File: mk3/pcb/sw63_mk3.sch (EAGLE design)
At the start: 62 parts, among them J1 USB-C_2.0_SMT, Q1 LGE2305, Q2 BC817S, Q3 BC817S, SW1 KSC321JLFS, SW2 EVQ-P7J01P, U1 ATSAMD21E18A-MU, U2 DS3231MZ+, U3 TLC5916IPW, U4 TLC5916IPW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

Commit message: finishing schematics
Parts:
- removed LD13, LD14, LD15, LD16: (no value), BASTL_LEDS:LED_THT-5MM_ALT
- removed LD17, LD18, LD19, LD20: LED_RECT-3.2X2, BASTL_LEDS:LED_RECT-3.2X2
- removed LD21: (no value), BASTL_LEDS:LED_THT-3MM_ALT
- removed LD22: LED_SMT_0805, BASTL_LEDS:LED_SMT_0805
- added B+, B-: TEST_PIN_LARGE, BASTL_PINHEADERS:TEST_PIN_LARGE
- added DOWN, LEFT, RIGHT, UP: LED_RECT-3.2X2, BASTL_LEDS:LED_RECT-3.2X2
- added HOURS, MINUS, MINUTES, PLUS: (no value), BASTL_LEDS:LED_THT-5MM_ALT
- added PM: (no value), BASTL_LEDS:LED_THT-3MM_ALT
- added Q4: TEMT6200FX01, BASTL_TRANZISTORS:TEMT6200FX01
- added R14: 10k, BASTL_RESISTORS:RESISTOR0603
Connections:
- new net LIGHT_SENS: Q4.E, R14.2, U1.PA02
- new net N$20: LD10.C, U3.OUT1
- new net N$25: LD5.C, U3.OUT7
- new net N$26: C9.2, U1.VDDCORE
- new net N$27: LD4.C, U4.OUT4
- new net N$28: LD3.C, U4.OUT5
- new net N$29: LD2.C, U4.OUT6
- new net N$31: MINUTES.C, U4.OUT3
- new net N$32: HOURS.C, U4.OUT2
- new net N$33: MINUS.C, U4.OUT1
- new net N$34: PLUS.C, U4.OUT0
- new net SCL: R5.2, U1.PA09, U2.SCL
- new net SDA: R6.2, U1.PA08, U2.SDA
- new net SWCLK: SWD.4, U1.PA30
- new net SWDIO: SWD.2, U1.PA31
- net !CHARGING: now also U1.PA10
- net !RESET: now also SWD.3
- net ACTIVE: now also Q4.C, U1.PA03
- net BAT: now also B+.P$1
- net BRIGHT: now also U1.PA18
- net BTN: now also U1.PA00
- net CLK: now also U1.PA07
- net D+: now also U1.PA27
- net D-: now also U1.PA25
- net DAT: now also U1.PA06
- net GND: now also B-.P$1, C10.1, C11.1, C9.1, R14.1, SWD.5, U1.EP, U1.GND
- net LAT: now also U1.PA05
- net N$15: now also PM.C; no longer LD21.C
- net N$16: now also DOWN.C; no longer LD19.C
- net N$17: now also LEFT.C; no longer LD20.C
- net N$18: now also RIGHT.C; no longer LD18.C
- net N$19: now also UP.C; no longer LD17.C
- net N$21: now also LD9.C, U3.OUT0; no longer LD13.C, U3.OUT2
- net N$22: now also LD8.C, U3.OUT4; no longer LD14.C, U3.OUT1
- net N$23: now also LD7.C, U3.OUT5; no longer LD15.C, U3.OUT0
- net N$24: now also LD6.C, U3.OUT6; no longer LD16.C, U3.OUT3
- net N$5: now also LD12.C, U3.OUT3; no longer R6.2, U2.SDA
- net N$7: now also LD11.C, U3.OUT2; no longer R5.2, U2.SCL
- net VBUS_DTCT: now also U1.PA04
- net VDD: now also C10.2, C11.2, SWD.1, U1.VDDANA, U1.VDDIN
- net VDDLEDS: now also DOWN.A, HOURS.A, LEFT.A, MINUS.A, MINUTES.A, PLUS.A, PM.A, RIGHT.A, UP.A; no longer LD13.A, LD14.A, LD15.A, LD16.A, LD17.A, LD18.A, LD19.A, LD20.A, LD21.A
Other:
- moved on the sheet: C10, C11, C9, LD1, LD10, LD11, LD12, LD2, LD3, LD4, LD5, LD6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

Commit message: routing done
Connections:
- net GND: now also U1.PA22
- net N$31: now also HOURS.C; no longer MINUTES.C
- net N$32: now also MINUTES.C; no longer HOURS.C
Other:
- note added: "Just for layout."
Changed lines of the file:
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@@
 <part name="B-" library="BASTL_PINHEADERS" library_urn="urn:adsk.eagle:library:32976504" deviceset="TEST_PIN" device="_LARGE" package3d_urn="urn:adsk.eagle:package:43479613/3" value="TEST_PIN_LARGE"/>
 <part name="GND21" library="BASTL_SYMBOLS" library_urn="urn:adsk.eagle:library:32975873" deviceset="GND" device=""/>
+<part name="GND22" library="BASTL_SYMBOLS" library_urn="urn:adsk.eagle:library:32975873" deviceset="GND" device=""/>
 </parts>
 <sheets>
@@
 <plain>
 <text x="238.76" y="76.2" size="1.27" layer="94" ratio="12">Kinda weird but works.</text>
+<text x="24.384" y="-19.05" size="1.27" layer="94" ratio="12">Just for layout.</text>
 </plain>
 <instances>
@@
 <instance part="GND21" gate="1" x="-99.06" y="2.54" smashed="yes">
 <attribute name="VALUE" x="-101.6" y="0" size="1.778" layer="96"/>
+</instance>
+<instance part="GND22" gate="1" x="35.56" y="-22.86" smashed="yes">
+<attribute name="VALUE" x="33.02" y="-25.4" size="1.778" layer="96"/>
 </instance>
 </instances>
@@
 <pinref part="B-" gate="G$1" pin="P$1"/>
 <pinref part="GND21" gate="1" pin="GND"/>
+</segment>
+<segment>
+<pinref part="U1" gate="G$1" pin="PA22"/>
+<pinref part="GND22" gate="1" pin="GND"/>
+<wire x1="15.24" y1="-20.32" x2="35.56" y2="-20.32" width="0.1524" layer="91"/>
 </segment>
 </net>
@@
 <wire x1="58.42" y1="73.66" x2="53.34" y2="73.66" width="0.1524" layer="91"/>
 <wire x1="53.34" y1="73.66" x2="53.34" y2="45.72" width="0.1524" layer="91"/>
-<pinref part="MINUTES" gate="G$1" pin="C"/>
-<wire x1="53.34" y1="45.72" x2="63.5" y2="45.72" width="0.1524" layer="91"/>
-<wire x1="63.5" y1="45.72" x2="63.5" y2="48.26" width="0.1524" layer="91"/>
+<pinref part="HOURS" gate="G$1" pin="C"/>
+<wire x1="53.34" y1="45.72" x2="71.12" y2="45.72" width="0.1524" layer="91"/>
+<wire x1="71.12" y1="45.72" x2="71.12" y2="48.26" width="0.1524" layer="91"/>
 </segment>
 </net>
@@
 <wire x1="58.42" y1="76.2" x2="50.8" y2="76.2" width="0.1524" layer="91"/>
 <wire x1="50.8" y1="76.2" x2="50.8" y2="43.18" width="0.1524" layer="91"/>
-<wire x1="50.8" y1="43.18" x2="71.12" y2="43.18" width="0.1524" layer="91"/>
-<pinref part="HOURS" gate="G$1" pin="C"/>
-<wire x1="71.12" y1="43.18" x2="71.12" y2="48.26" width="0.1524" layer="91"/>
-</segment>
-</net>
+<pinref part="MINUTES" gate="G$1" pin="C"/>
+<wire x1="50.8" y1="43.18" x2="63.5" y2="43.18" width="0.1524" layer="91"/>
+<wire x1="63.5" y1="43.18" x2="63.5" y2="48.26" width="0.1524" layer="91"/>
+</segment>
+</net>

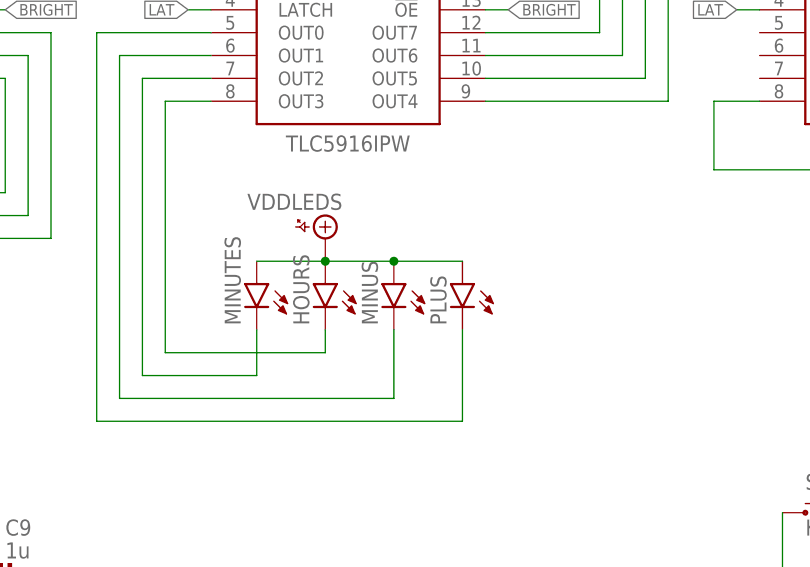
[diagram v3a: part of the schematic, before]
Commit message: update led colors to match reality
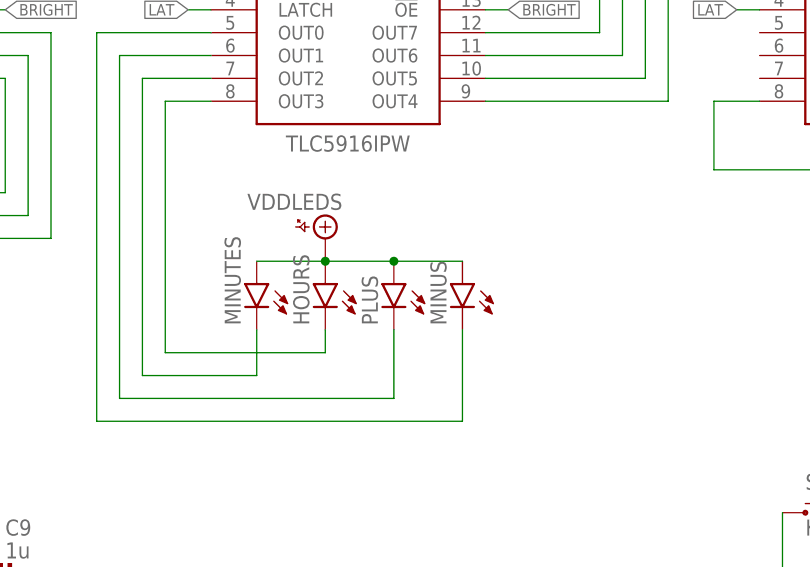
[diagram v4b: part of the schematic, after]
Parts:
- HOURS: device BASTL_LEDS:LED_THT-5MM_ALT -> BASTL_LEDS:LED_THT-5MM_B
- MINUS: device BASTL_LEDS:LED_THT-5MM_ALT -> BASTL_LEDS:LED_THT-5MM_R
- MINUTES: device BASTL_LEDS:LED_THT-5MM_ALT -> BASTL_LEDS:LED_THT-5MM_Y
- PLUS: device BASTL_LEDS:LED_THT-5MM_ALT -> BASTL_LEDS:LED_THT-5MM_G
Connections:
- net N$33: now also PLUS.C; no longer MINUS.C
- net N$34: now also MINUS.C; no longer PLUS.C
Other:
- moved on the sheet: MINUS, PLUS
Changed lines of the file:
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@@
 <part name="LD11" library="BASTL_LEDS" library_urn="urn:adsk.eagle:library:32977677" deviceset="LED_SMT" device="_1206" package3d_urn="urn:adsk.eagle:package:45095787/2"/>
 <part name="LD12" library="BASTL_LEDS" library_urn="urn:adsk.eagle:library:32977677" deviceset="LED_SMT" device="_1206" package3d_urn="urn:adsk.eagle:package:45095787/2"/>
-<part name="PLUS" library="BASTL_LEDS" library_urn="urn:adsk.eagle:library:32977677" deviceset="LED_THT" device="-5MM_ALT" package3d_urn="urn:adsk.eagle:package:45095770/2"/>
-<part name="MINUS" library="BASTL_LEDS" library_urn="urn:adsk.eagle:library:32977677" deviceset="LED_THT" device="-5MM_ALT" package3d_urn="urn:adsk.eagle:package:45095770/2"/>
-<part name="HOURS" library="BASTL_LEDS" library_urn="urn:adsk.eagle:library:32977677" deviceset="LED_THT" device="-5MM_ALT" package3d_urn="urn:adsk.eagle:package:45095770/2"/>
-<part name="MINUTES" library="BASTL_LEDS" library_urn="urn:adsk.eagle:library:32977677" deviceset="LED_THT" device="-5MM_ALT" package3d_urn="urn:adsk.eagle:package:45095770/2"/>
+<part name="MINUS" library="BASTL_LEDS" library_urn="urn:adsk.eagle:library:32977677" deviceset="LED_THT" device="-5MM_R" package3d_urn="urn:adsk.eagle:package:45109722/2"/>
+<part name="PLUS" library="BASTL_LEDS" library_urn="urn:adsk.eagle:library:32977677" deviceset="LED_THT" device="-5MM_G" package3d_urn="urn:adsk.eagle:package:45109721/2"/>
+<part name="HOURS" library="BASTL_LEDS" library_urn="urn:adsk.eagle:library:32977677" deviceset="LED_THT" device="-5MM_B" package3d_urn="urn:adsk.eagle:package:45109720/2"/>
+<part name="MINUTES" library="BASTL_LEDS" library_urn="urn:adsk.eagle:library:32977677" deviceset="LED_THT" device="-5MM_Y" package3d_urn="urn:adsk.eagle:package:45109719/2"/>
 <part name="UP" library="BASTL_LEDS" library_urn="urn:adsk.eagle:library:32977677" deviceset="LED_RECT" device="-3.2X2" package3d_urn="urn:adsk.eagle:package:45095773/2"/>
 <part name="RIGHT" library="BASTL_LEDS" library_urn="urn:adsk.eagle:library:32977677" deviceset="LED_RECT" device="-3.2X2" package3d_urn="urn:adsk.eagle:package:45095773/2"/>
@@
 <attribute name="NAME" x="-23.876" y="135.128" size="1.778" layer="95" rot="MR90"/>
 </instance>
-<instance part="PLUS" gate="G$1" x="86.36" y="53.34" smashed="yes" rot="MR0">
+<instance part="MINUS" gate="G$1" x="86.36" y="53.34" smashed="yes" rot="MR0">
 <attribute name="NAME" x="82.804" y="48.768" size="1.778" layer="95" rot="MR90"/>
 <attribute name="VALUE" x="80.645" y="48.768" size="1.778" layer="96" rot="MR90"/>
 </instance>
-<instance part="MINUS" gate="G$1" x="78.74" y="53.34" smashed="yes" rot="MR0">
+<instance part="PLUS" gate="G$1" x="78.74" y="53.34" smashed="yes" rot="MR0">
 <attribute name="NAME" x="75.184" y="48.768" size="1.778" layer="95" rot="MR90"/>
 <attribute name="VALUE" x="73.025" y="48.768" size="1.778" layer="96" rot="MR90"/>
@@
 <segment>
 <pinref part="MINUTES" gate="G$1" pin="A"/>
+<pinref part="MINUS" gate="G$1" pin="A"/>
+<wire x1="86.36" y1="55.88" x2="78.74" y2="55.88" width="0.1524" layer="91"/>
 <pinref part="PLUS" gate="G$1" pin="A"/>
-<wire x1="86.36" y1="55.88" x2="78.74" y2="55.88" width="0.1524" layer="91"/>
-<pinref part="MINUS" gate="G$1" pin="A"/>
 <junction x="78.74" y="55.88"/>
 <wire x1="78.74" y1="55.88" x2="71.12" y2="55.88" width="0.1524" layer="91"/>
@@
 <wire x1="48.26" y1="78.74" x2="48.26" y2="40.64" width="0.1524" layer="91"/>
 <wire x1="48.26" y1="40.64" x2="78.74" y2="40.64" width="0.1524" layer="91"/>
-<pinref part="MINUS" gate="G$1" pin="C"/>
+<pinref part="PLUS" gate="G$1" pin="C"/>
 <wire x1="78.74" y1="40.64" x2="78.74" y2="48.26" width="0.1524" layer="91"/>
 </segment>
@@
 <wire x1="45.72" y1="81.28" x2="58.42" y2="81.28" width="0.1524" layer="91"/>
 <wire x1="86.36" y1="38.1" x2="86.36" y2="48.26" width="0.1524" layer="91"/>
-<pinref part="PLUS" gate="G$1" pin="C"/>
-</segment>
-</net>
+<pinref part="MINUS" gate="G$1" pin="C"/>
+</segment>
+</net>

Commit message: board update
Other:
- note added: "TODO FIX: PA25->D+ PA24->D-"
- note added: "TODO FIX: VBAT -> GND VCC -> VDD"
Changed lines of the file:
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@@
 <layer number="96" name="Values" color="7" fill="1" visible="yes" active="yes"/>
 <layer number="97" name="Info" color="7" fill="1" visible="yes" active="yes"/>
-<layer number="98" name="Guide" color="6" fill="1" visible="yes" active="yes"/>
+<layer number="98" name="Guide" color="63" fill="1" visible="yes" active="yes"/>
 <layer number="99" name="SpiceOrder" color="7" fill="1" visible="yes" active="yes"/>
 <layer number="100" name="Muster" color="7" fill="1" visible="no" active="yes"/>
@@
 <text x="238.76" y="76.2" size="1.27" layer="94" ratio="12">Kinda weird but works.</text>
 <text x="24.384" y="-19.05" size="1.27" layer="94" ratio="12">Just for layout.</text>
+<text x="81.28" y="10.16" size="3.048" layer="98">TODO FIX:
+VBAT -&gt; GND
+VCC -&gt; VDD</text>
+<text x="25.4" y="-48.26" size="3.048" layer="98">TODO FIX:
+PA25-&gt;D+
+PA24-&gt;D-</text>
 </plain>
 <instances>
@@
 </drawing>
 <compatibility>
+<note version="6.3" minversion="6.2.2" severity="warning">
+Since Version 6.2.2 text objects can contain more than one line,
+which will not be processed correctly with this version.
+</note>
 <note version="8.2" severity="warning">
 Since Version 8.2, EAGLE supports online libraries. The ids

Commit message: schematic notes
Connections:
- net N$6 renamed VSEL
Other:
- note added: "REWORK THIS SECTION: REPLACE VBUS_FUSED WITH VSEL"
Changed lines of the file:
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@@
 PA25-&gt;D+
 PA24-&gt;D-</text>
+<text x="231.14" y="106.68" size="3.048" layer="98">REWORK THIS SECTION:
+REPLACE VBUS_FUSED
+WITH VSEL</text>
 </plain>
 <instances>
@@
 </segment>
 </net>
-<net name="N$6" class="0">
+<net name="VSEL" class="0">
 <segment>
 <pinref part="D1" gate="G$1" pin="C"/>
@@
 <pinref part="C3" gate="G$1" pin="1"/>
 <junction x="-144.78" y="-68.58"/>
-</segment>
-</net>
+<label x="-139.7" y="-63.5" size="1.778" layer="95" rot="R90" xref="yes"/>
+</segment>
+</net>
